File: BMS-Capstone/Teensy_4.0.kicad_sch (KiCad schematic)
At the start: 0 parts

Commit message: added resistor
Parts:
- added R1: R, symbol Device:R
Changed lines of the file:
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@@
 	(generator_version "9.0")
 	(paper "A4")
+	(symbol
+		(lib_id "Device:R")
+		(at 154.94 85.09 0)
+		(unit 1)
+		(exclude_from_sim no)
+		(in_bom yes)
+		(on_board yes)
+		(dnp no)
+		(fields_autoplaced yes)
+		(property "Reference" "R1"
+			(at 157.48 83.8199 0)
+			(effects
+				(font
+					(size 1.27 1.27)
+				)
+				(justify left)
+			)
+		)
+		(property "Value" "R"
+			(at 157.48 86.3599 0)
+			(effects
+				(font
+					(size 1.27 1.27)
+				)
+				(justify left)
+			)
+		)
+		(property "Footprint" ""
+			(at 153.162 85.09 90)
+			(effects
+				(font
+					(size 1.27 1.27)
+				)
+				(hide yes)
+			)
+		)
+		(property "Datasheet" "~"
+			(at 154.94 85.09 0)
+			(effects
+				(font
+					(size 1.27 1.27)
+				)
+				(hide yes)
+			)
+		)
+		(property "Description" "Resistor"
+			(at 154.94 85.09 0)
+			(effects
+				(font
+					(size 1.27 1.27)
+				)
+				(hide yes)
+			)
+		)
+		(pin "1"
+		)
+		(pin "2"
+		)
+		(instances
+			(project ""
+				(path "/f2da9442-ca05-4687-a880-d5cd24c39f1d/26bdc180-da09-44b1-8397-e88b39d0135c"
+					(reference "R1")
+					(unit 1)
+				)
+			)
+		)
+	)
 )

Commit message: Finished teensy
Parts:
- removed R1: R, symbol Device:R
- added U1: Teensy4.0, teensy.pretty-master:Teensy40_SMT, symbol teensy:Teensy4.0
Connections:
- new net 3V3: U1.33 (VIN)
- new net GND: U1.1 (GND), U1.17 (GND), U1.32 (GND), U1.47 (GND)
- new net SCL0: U1.26 (19_A5_SCL0)
- new net SCL1: U1.23 (16_A2_RX4_SCL1)
- new net SDA0: U1.25 (18_A4_SDA0)
- new net SDA1: U1.24 (17_A3_TX4_SDA1)

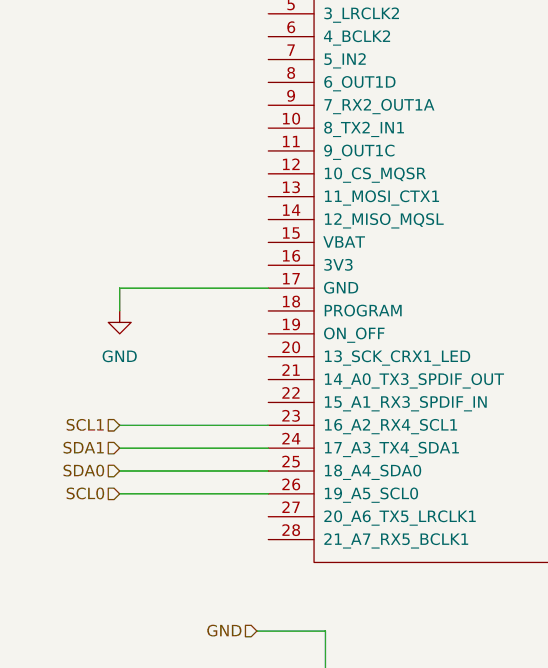
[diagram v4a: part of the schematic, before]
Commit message: Integrated in Monitoring board into final pcb
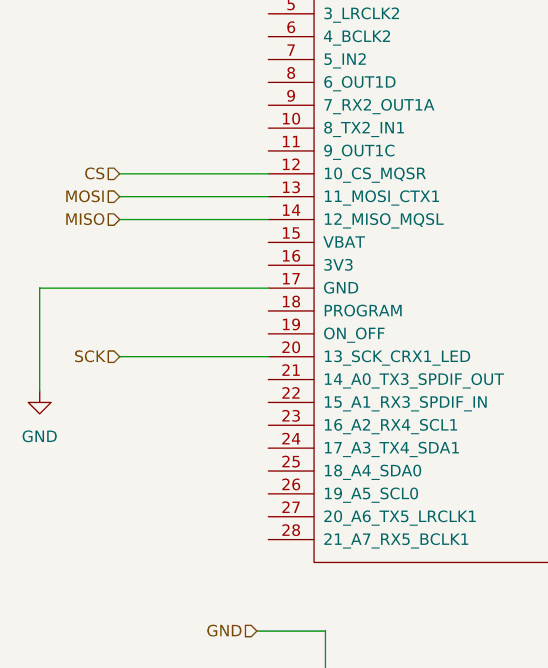
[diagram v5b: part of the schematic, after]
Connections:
- net CS: now reaches U1.12 (10_CS_MQSR)
- net MOSI: now reaches U1.13 (11_MOSI_CTX1)
- net MISO: now reaches U1.14 (12_MISO_MQSL)
- net SCK: now reaches U1.20 (13_SCK_CRX1_LED)
- net SCL0: no longer names the net of U1.26 (19_A5_SCL0)
- net SCL1: no longer names the net of U1.23 (16_A2_RX4_SCL1)
- net SDA0: no longer names the net of U1.25 (18_A4_SDA0)
- net SDA1: no longer names the net of U1.24 (17_A3_TX4_SDA1)
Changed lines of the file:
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@@
 	(wire
 		(pts
-			(xy 127 116.84) (xy 110.49 116.84)
+			(xy 127 86.36) (xy 110.49 86.36)
 		)
 		(stroke
@@
 	(wire
 		(pts
-			(xy 110.49 93.98) (xy 110.49 96.52)
-		)
-		(stroke
-			(width 0)
-			(type default)
-		)
-	)
-	(wire
-		(pts
-			(xy 110.49 111.76) (xy 127 111.76)
-		)
-		(stroke
-			(width 0)
-			(type default)
-		)
-	)
-	(wire
-		(pts
-			(xy 110.49 109.22) (xy 127 109.22)
-		)
-		(stroke
-			(width 0)
-			(type default)
-		)
-	)
-	(wire
-		(pts
-			(xy 110.49 93.98) (xy 127 93.98)
+			(xy 101.6 93.98) (xy 101.6 105.41)
+		)
+		(stroke
+			(width 0)
+			(type default)
+		)
+	)
+	(wire
+		(pts
+			(xy 110.49 81.28) (xy 127 81.28)
+		)
+		(stroke
+			(width 0)
+			(type default)
+		)
+	)
+	(wire
+		(pts
+			(xy 110.49 101.6) (xy 127 101.6)
+		)
+		(stroke
+			(width 0)
+			(type default)
+		)
+	)
+	(wire
+		(pts
+			(xy 101.6 93.98) (xy 127 93.98)
 		)
 		(stroke
@@
 	(wire
 		(pts
-			(xy 110.49 114.3) (xy 127 114.3)
+			(xy 110.49 83.82) (xy 127 83.82)
 		)
 		(stroke
@@
 		)
 	)
-	(hierarchical_label "SCL0"
-		(shape input)
-		(at 110.49 116.84 180)
-		(effects
-			(font
-				(size 1.27 1.27)
-			)
-			(justify right)
-		)
-	)
-	(hierarchical_label "SCL1"
-		(shape input)
-		(at 110.49 109.22 180)
+	(hierarchical_label "MISO"
+		(shape input)
+		(at 110.49 86.36 180)
+		(effects
+			(font
+				(size 1.27 1.27)
+			)
+			(justify right)
+		)
+	)
+	(hierarchical_label "SCK"
+		(shape input)
+		(at 110.49 101.6 180)
 		(effects
 			(font
@@
 		)
 	)
-	(hierarchical_label "SDA1"
-		(shape input)
-		(at 110.49 111.76 180)
-		(effects
-			(font
-				(size 1.27 1.27)
-			)
-			(justify right)
-		)
-	)
-	(hierarchical_label "SDA0"
-		(shape input)
-		(at 110.49 114.3 180)
+	(hierarchical_label "CS"
+		(shape input)
+		(at 110.49 81.28 180)
+		(effects
+			(font
+				(size 1.27 1.27)
+			)
+			(justify right)
+		)
+	)
+	(hierarchical_label "MOSI"
+		(shape input)
+		(at 110.49 83.82 180)
 		(effects
 			(font
@@
 	(symbol
 		(lib_id "power:GND")
-		(at 110.49 96.52 0)
+		(at 101.6 105.41 0)
 		(unit 1)
 		(exclude_from_sim no)
@@
 		(fields_autoplaced yes)
 		(property "Reference" "#PWR09"
-			(at 110.49 102.87 0)
+			(at 101.6 111.76 0)
 			(effects
 				(font
@@
 		)
 		(property "Value" "GND"
-			(at 110.49 101.6 0)
+			(at 101.6 110.49 0)
 			(effects
 				(font
@@
 		)
 		(property "Footprint" ""
-			(at 110.49 96.52 0)
+			(at 101.6 105.41 0)
 			(effects
 				(font
@@
 		)
 		(property "Datasheet" ""
-			(at 110.49 96.52 0)
+			(at 101.6 105.41 0)
 			(effects
 				(font
@@
 		)
 		(property "Description" "Power symbol creates a global label with name \"GND\" , ground"
-			(at 110.49 96.52 0)
-			(effects
-				(font
+			(at 101.6 105.41 0)
+			(effects
+				(font
